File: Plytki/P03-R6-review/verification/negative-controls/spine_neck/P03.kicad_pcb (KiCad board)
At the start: 2 copper layers, 160 x 100 mm, 134 parts, among them M1 Waveshare N32R16V, Q1 AO3401A, U1 MCP23017-E/SP, U11 74LVC125A, U12 74LVC125A, U13 74LVC125A, U14 74LVC125A, U2 SN74HC139N, U21 74LVC125A, U22 74LVC125A, U23 74LVC125A, U3 TPS3808G33, U4 SN74LVC1G37DBVR, U5 LTC4412IS6, U6 SN74LVC1G17DBVR

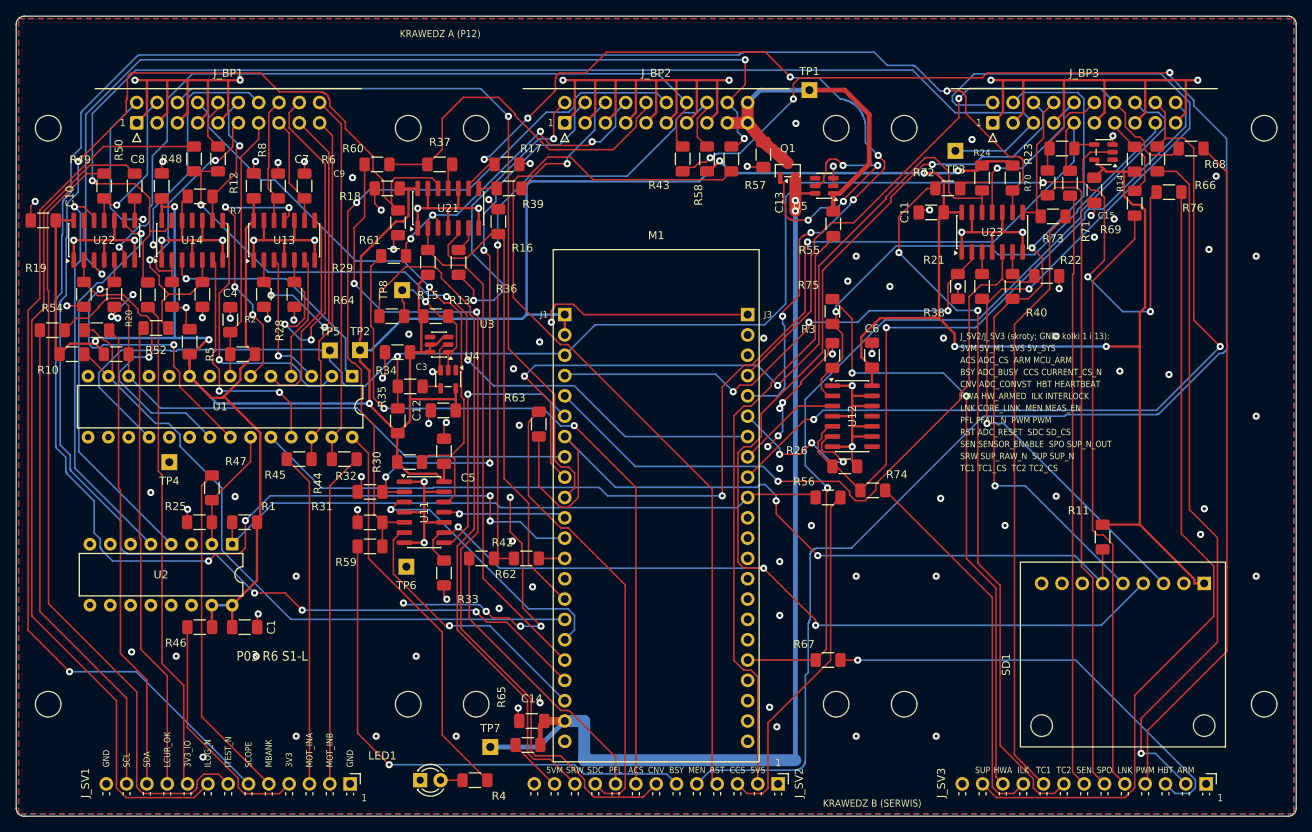
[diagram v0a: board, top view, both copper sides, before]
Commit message: P03 R6 PCB: poprawki po recenzji 1.10 i nowe trasowanie
- R70 10 kΩ (gałąź serwisowa SUP_N_OUT; verify_reset liczy gałąź, mutacja R70 = 1 kΩ)
- listwy: szyna tylko obok GND, innej szyny albo linii za 10 kΩ (verify_jbp C12),
  odwołania J_SVn.p w ODBIOR sprawdzane (C13); kolejność bliska trasowalnej z 30.09
- skrót ADC_RESET „ARS”, GND opisane na obu końcach J_SV2/J_SV3 (napis przy kołku 1
  nad znacznikiem pinu), legenda skrótów jako naklejka (docs/NAKLEJKA-SERWIS.md),
  STANY-DOMYSLNE.csv z tabel verify_function.py, tytuł z klasą i slotami
- verify_pcb: pas zastrzeżony krawędzi A, bliskość oznaczeń, lib_footprint_mismatch
  tylko przy polach równych bibliotece, raport tras planera; nowe próby ujemne
- nowe trasowanie (pierwsza próba): DRC 0/0/0 (6 przyjętych lib_footprint_mismatch),
  kontrole PCB 27/27, próby ujemne 25/25, 242 przelotki; README i STAN-PRAC

Co-Authored-By: Claude Opus 5.5 <noreply@anthropic.com>
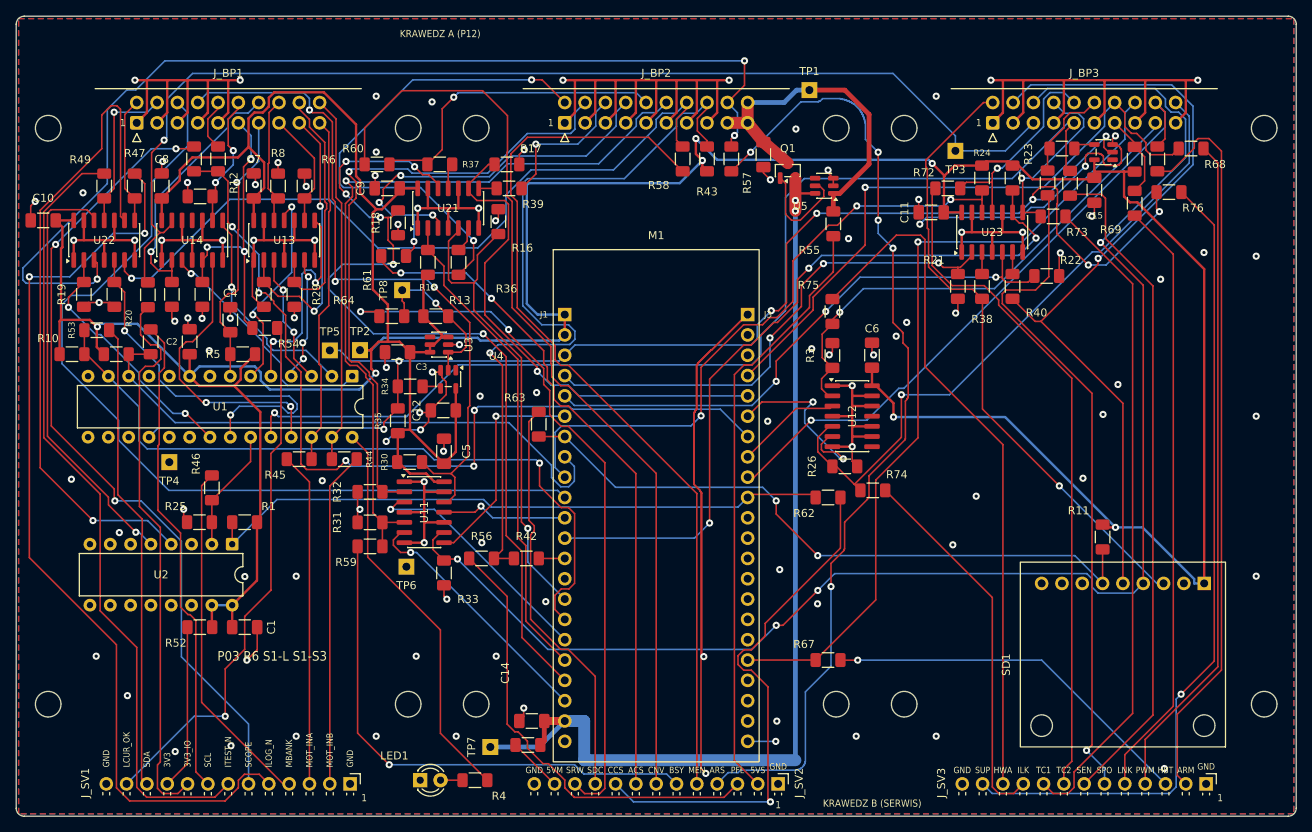
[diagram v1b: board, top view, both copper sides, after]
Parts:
- R50, R56, R70: value 1K / 1% 1206 -> 10K / 1% 1206
- R54, R62: value 10K / 1% 1206 -> 1K / 1% 1206
- moved R56 44.0 mm to (58.2, 67.8), turned to 180 degrees
- moved R62 44.0 mm to (101.5, 60.2), turned to 0 degrees
- moved R47 38.9 mm to (14.8, 21.2)
- moved R52 37.8 mm to (22.9, 76.4)
- moved R54 26.6 mm to (31.1, 39.0), turned to 0 degrees
- moved R50 19.6 mm to (16.8, 40.7)
- moved R46 17.5 mm to (24.5, 59.0), turned to 90 degrees
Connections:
- J_SV1 pad 10: /SERWIS/SV_LOGGER_CURRENT_OK -> /SERWIS/SV_3V3_CORE
- J_SV1 pad 12: /SERWIS/SV_I2C_SCL -> /SERWIS/SV_LOGGER_CURRENT_OK
- J_SV1 pad 4: /SERWIS/SV_3V3_CORE -> /SERWIS/SV_MEAS_BANK
- J_SV1 pad 5: /SERWIS/SV_MEAS_BANK -> /SERWIS/SV_CS_ILOG_N
- J_SV1 pad 8: /SERWIS/SV_CS_ILOG_N -> /SERWIS/SV_I2C_SCL
- J_SV2 pad 3: /SERWIS/SV_CURRENT_CS_N -> /SERWIS/SV_PFAIL_N
- J_SV2 pad 9: /SERWIS/SV_PFAIL_N -> /SERWIS/SV_CURRENT_CS_N
- R46 pad 1: 3V3_CORE -> MEAS_BANK
- R46 pad 2: /SERWIS/SV_3V3_CORE -> /SERWIS/SV_MEAS_BANK
- R47 pad 1: MEAS_BANK -> CS_ILOG_N
- R47 pad 2: /SERWIS/SV_MEAS_BANK -> /SERWIS/SV_CS_ILOG_N
- R50 pad 1: CS_ILOG_N -> I2C_SCL
- R50 pad 2: /SERWIS/SV_CS_ILOG_N -> /SERWIS/SV_I2C_SCL
- R52 pad 1: LOGGER_CURRENT_OK -> 3V3_CORE
- R52 pad 2: /SERWIS/SV_LOGGER_CURRENT_OK -> /SERWIS/SV_3V3_CORE
- R54 pad 1: I2C_SCL -> LOGGER_CURRENT_OK
- R54 pad 2: /SERWIS/SV_I2C_SCL -> /SERWIS/SV_LOGGER_CURRENT_OK
- R56 pad 1: CURRENT_CS_N -> PFAIL_N
- R56 pad 2: /SERWIS/SV_CURRENT_CS_N -> /SERWIS/SV_PFAIL_N
- R62 pad 1: PFAIL_N -> CURRENT_CS_N
- R62 pad 2: /SERWIS/SV_PFAIL_N -> /SERWIS/SV_CURRENT_CS_N
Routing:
- net TC1_CS_SRC: track 261.3 -> 94.1 mm, vias 5 -> 3
- net /SERWIS/SV_MEAS_EN: track 208.8 -> 113.1 mm, vias 3 -> 0
- net GND: track 475.7 -> 551.5 mm, vias 119 -> 108
- net ADC_CONVST_SRC: track 183.3 -> 111.5 mm, vias 4 -> 6
- net ADC_SDI_SRC: track 110.5 -> 63.3 mm, vias 7 -> 1
- net SPI3_SCLK: track 122.2 -> 78.6 mm, vias 2 -> 1
- net CS_ILOG_N_SRC: track 50.2 -> 84.7 mm
- net 3V3_CORE: track 497.5 -> 526.5 mm, vias 9 -> 7
- net SUP_N: track 209.4 -> 186.3 mm, vias 4 -> 8
- net ADC_SCLK: track 39.2 -> 61.7 mm
- net MCU_ARM: track 102.5 -> 80.3 mm, vias 2 -> 1
- net /SERWIS/SV_CURRENT_CS_N: track 44.7 -> 66.4 mm, vias 0 -> 1
- net 3V3_IO: track 165.0 -> 143.7 mm
- net /SERWIS/SV_PFAIL_N: track 36.4 -> 57.0 mm
- net SCOPE_TRIG: track 90.8 -> 109.9 mm, vias 3 -> 5
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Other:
- board text added: "ARS"
- board text added: "P03 R6 S1-L S1-S3"
- board text removed: "5VM 5V_M1 5VS 5V_SYS"
- board text removed: "ACS ADC_CS ARM MCU_ARM"
- board text removed: "BSY ADC_BUSY CCS CURRENT_CS_N"
- board text removed: "CNV ADC_CONVST HBT HEARTBEAT"
- board text removed: "HWA HW_ARMED ILK INTERLOCK"
- board text removed: "J_SV2/J_SV3 (skroty; GND: kolki 1 i 13):"
- board text removed: "LNK CORE_LINK MEN MEAS_EN"
- board text removed: "P03 R6 S1-L"
- board text removed: "PFL PFAIL_N PWM PWM"
- board text removed: "RST"
- board text removed: "RST ADC_RESET SDC SD_CS"
- board text removed: "SEN SENSOR_ENABLE SPO SUP_N_OUT"
- board text removed: "SRW SUP_RAW_N SUP SUP_N"
- board text removed: "TC1 TC1_CS TC2 TC2_CS"
